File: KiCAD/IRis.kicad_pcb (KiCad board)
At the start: 2 copper layers, 31.3 x 31.3 mm, 28 parts, among them P1 Digital Out, Q1 MMBF4117, Q2 MMBF4117, Q3 MMBF4117, U1 TSV911ILT, U2 TLV3201

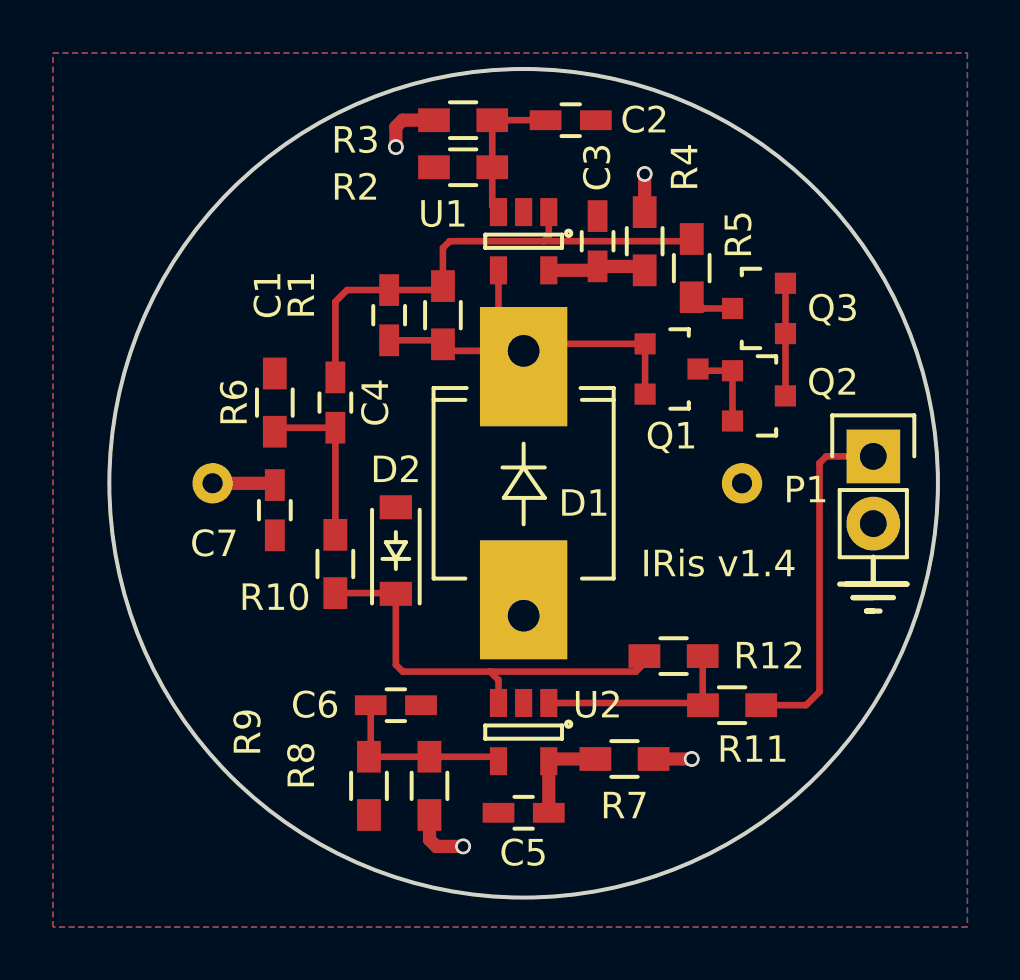
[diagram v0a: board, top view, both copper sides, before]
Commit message: Added test points TP1 and TP2 for monitoring the signal before and after DC blocking capacitor C4.
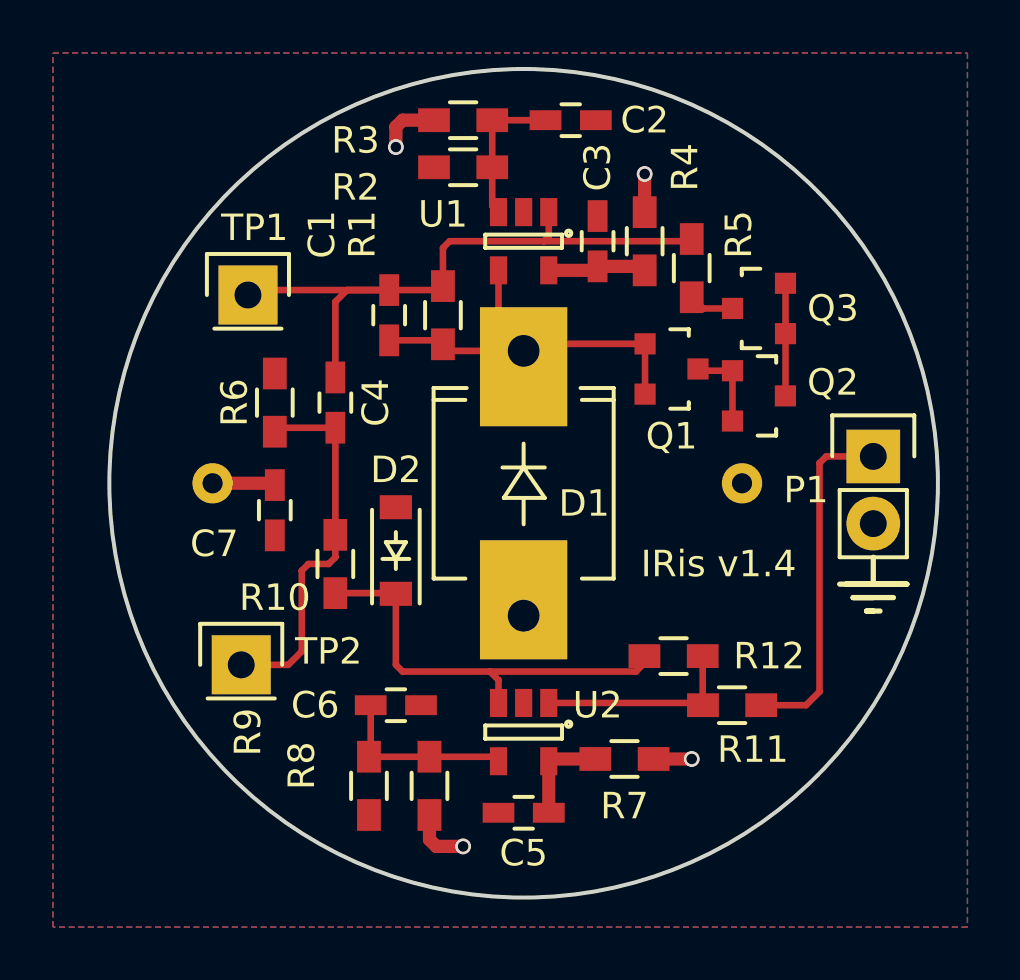
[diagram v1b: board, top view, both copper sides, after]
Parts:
- added TP1: Test Point #1, Pin_Headers:Pin_Header_Straight_1x01, F.Cu at (131.8, 92.5)
- added TP2: Test Point #2, Pin_Headers:Pin_Header_Straight_1x01, F.Cu at (131.6, 106.4)
- R5: value 100 -> 0
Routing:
- net Net-(C4-Pad1): track 6.39 -> 14.3 mm
- net Net-(C1-Pad1): track 19.6 -> 25.1 mm
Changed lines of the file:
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@@
 (kicad_pcb (version 4) (host pcbnew 4.0.2-stable)
   (general
-    (links 50)
+    (links 52)
     (no_connects 0)
     (area 124.46 82.827 159.794429 116.332001)
     (thickness 1.6)
     (drawings 15)
-    (tracks 92)
+    (tracks 101)
     (zones 0)
-    (modules 28)
+    (modules 30)
     (nets 16)
   )
@@
     (tags "capacitor 0603")
     (attr smd)
-    (fp_text reference C1 (at -0.762 4.572 270) (layer F.SilkS)
+    (fp_text reference C1 (at -3.048 2.54 270) (layer F.SilkS)
       (effects (font (size 1 1) (thickness 0.15)))
     )
@@
     (tags "resistor 0603")
     (attr smd)
-    (fp_text reference R1 (at -0.762 5.334 270) (layer F.SilkS)
+    (fp_text reference R1 (at -3.048 3.048 270) (layer F.SilkS)
       (effects (font (size 1 1) (thickness 0.15)))
     )
@@
       (effects (font (size 1 1) (thickness 0.15)))
     )
-    (fp_text value 100 (at 0 1.9 90) (layer F.Fab)
+    (fp_text value 0 (at 0 1.9 90) (layer F.Fab)
       (effects (font (size 1 1) (thickness 0.15)))
     )
@@
     )
   )
+  (module Pin_Headers:Pin_Header_Straight_1x01 (layer F.Cu)
+    (at 131.826 92.456)
+    (descr "Through hole pin header")
+    (tags "pin header")
+    (fp_text reference TP1 (at 0.254 -2.54) (layer F.SilkS)
+      (effects (font (size 1 1) (thickness 0.15)))
+    )
+    (fp_text value "Test Point #1" (at 0 -3.1) (layer F.Fab)
+      (effects (font (size 1 1) (thickness 0.15)))
+    )
+    (fp_line (start 1.55 -1.55) (end 1.55 0) (layer F.SilkS) (width 0.15))
+    (fp_line (start -1.75 -1.75) (end -1.75 1.75) (layer F.CrtYd) (width 0.05))
+    (fp_line (start 1.75 -1.75) (end 1.75 1.75) (layer F.CrtYd) (width 0.05))
+    (fp_line (start -1.75 -1.75) (end 1.75 -1.75) (layer F.CrtYd) (width 0.05))
+    (fp_line (start -1.75 1.75) (end 1.75 1.75) (layer F.CrtYd) (width 0.05))
+    (fp_line (start -1.55 0) (end -1.55 -1.55) (layer F.SilkS) (width 0.15))
+    (fp_line (start -1.55 -1.55) (end 1.55 -1.55) (layer F.SilkS) (width 0.15))
+    (fp_line (start -1.27 1.27) (end 1.27 1.27) (layer F.SilkS) (width 0.15))
+    (pad 1 thru_hole rect (at 0 0) (size 2.2352 2.2352) (drill 1.016) (layers *.Cu *.Mask F.SilkS)
+      (net 1 "Net-(C1-Pad1)"))
+    (model Pin_Headers.3dshapes/Pin_Header_Straight_1x01.wrl
+      (at (xyz 0 0 0))
+      (scale (xyz 1 1 1))
+      (rotate (xyz 0 0 90))
+    )
+  )
+  (module Pin_Headers:Pin_Header_Straight_1x01 (layer F.Cu)
+    (at 131.572 106.426)
+    (descr "Through hole pin header")
+    (tags "pin header")
+    (fp_text reference TP2 (at 3.302 -0.508) (layer F.SilkS)
+      (effects (font (size 1 1) (thickness 0.15)))
+    )
+    (fp_text value "Test Point #2" (at 0 -3.1) (layer F.Fab)
+      (effects (font (size 1 1) (thickness 0.15)))
+    )
+    (fp_line (start 1.55 -1.55) (end 1.55 0) (layer F.SilkS) (width 0.15))
+    (fp_line (start -1.75 -1.75) (end -1.75 1.75) (layer F.CrtYd) (width 0.05))
+    (fp_line (start 1.75 -1.75) (end 1.75 1.75) (layer F.CrtYd) (width 0.05))
+    (fp_line (start -1.75 -1.75) (end 1.75 -1.75) (layer F.CrtYd) (width 0.05))
+    (fp_line (start -1.75 1.75) (end 1.75 1.75) (layer F.CrtYd) (width 0.05))
+    (fp_line (start -1.55 0) (end -1.55 -1.55) (layer F.SilkS) (width 0.15))
+    (fp_line (start -1.55 -1.55) (end 1.55 -1.55) (layer F.SilkS) (width 0.15))
+    (fp_line (start -1.27 1.27) (end 1.27 1.27) (layer F.SilkS) (width 0.15))
+    (pad 1 thru_hole rect (at 0 0) (size 2.2352 2.2352) (drill 1.016) (layers *.Cu *.Mask F.SilkS)
+      (net 6 "Net-(C4-Pad1)"))
+    (model Pin_Headers.3dshapes/Pin_Header_Straight_1x01.wrl
+      (at (xyz 0 0 0))
+      (scale (xyz 1 1 1))
+      (rotate (xyz 0 0 90))
+    )
+  )
   (gr_line (start 155.194 104.394) (end 155.702 104.394) (angle 90) (layer B.SilkS) (width 0.2))
   (gr_line (start 156.21 103.886) (end 154.686 103.886) (angle 90) (layer B.SilkS) (width 0.2))
@@
   )
   (gr_circle (center 142.24 99.568) (end 154.94 108.712) (layer Edge.Cuts) (width 0.15))
+  (segment (start 137.16 92.268) (end 132.014 92.268) (width 0.25) (layer F.Cu) (net 1) (status C00000))
+  (segment (start 132.014 92.268) (end 131.826 92.456) (width 0.25) (layer F.Cu) (net 1) (status C00000))
   (segment (start 137.16 92.268) (end 135.57 92.268) (width 0.25) (layer F.Cu) (net 1))
   (segment (start 135.128 92.71) (end 135.128 95.57) (width 0.25) (layer F.Cu) (net 1))
@@
   (segment (start 144.884 91.524) (end 145.034 91.374) (width 0.5) (layer F.Cu) (net 5))
   (segment (start 143.34 91.374) (end 143.19 91.524) (width 0.25) (layer F.Cu) (net 5))
+  (segment (start 131.572 106.426) (end 133.35 106.426) (width 0.25) (layer F.Cu) (net 6) (status 400000))
+  (segment (start 135.128 102.362) (end 135.128 101.516) (width 0.25) (layer F.Cu) (net 6) (status 800000))
+  (segment (start 134.874 102.616) (end 135.128 102.362) (width 0.25) (layer F.Cu) (net 6))
+  (segment (start 134.112 102.616) (end 134.874 102.616) (width 0.25) (layer F.Cu) (net 6))
+  (segment (start 133.858 102.87) (end 134.112 102.616) (width 0.25) (layer F.Cu) (net 6))
+  (segment (start 133.858 105.918) (end 133.858 102.87) (width 0.25) (layer F.Cu) (net 6))
+  (segment (start 133.35 106.426) (end 133.858 105.918) (width 0.25) (layer F.Cu) (net 6))
   (segment (start 135.128 97.47) (end 132.992 97.47) (width 0.25) (layer F.Cu) (net 6))
   (segment (start 132.992 97.47) (end 132.842 97.62) (width 0.25) (layer F.Cu) (net 6))

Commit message: Removed all vias from volterra PCB design
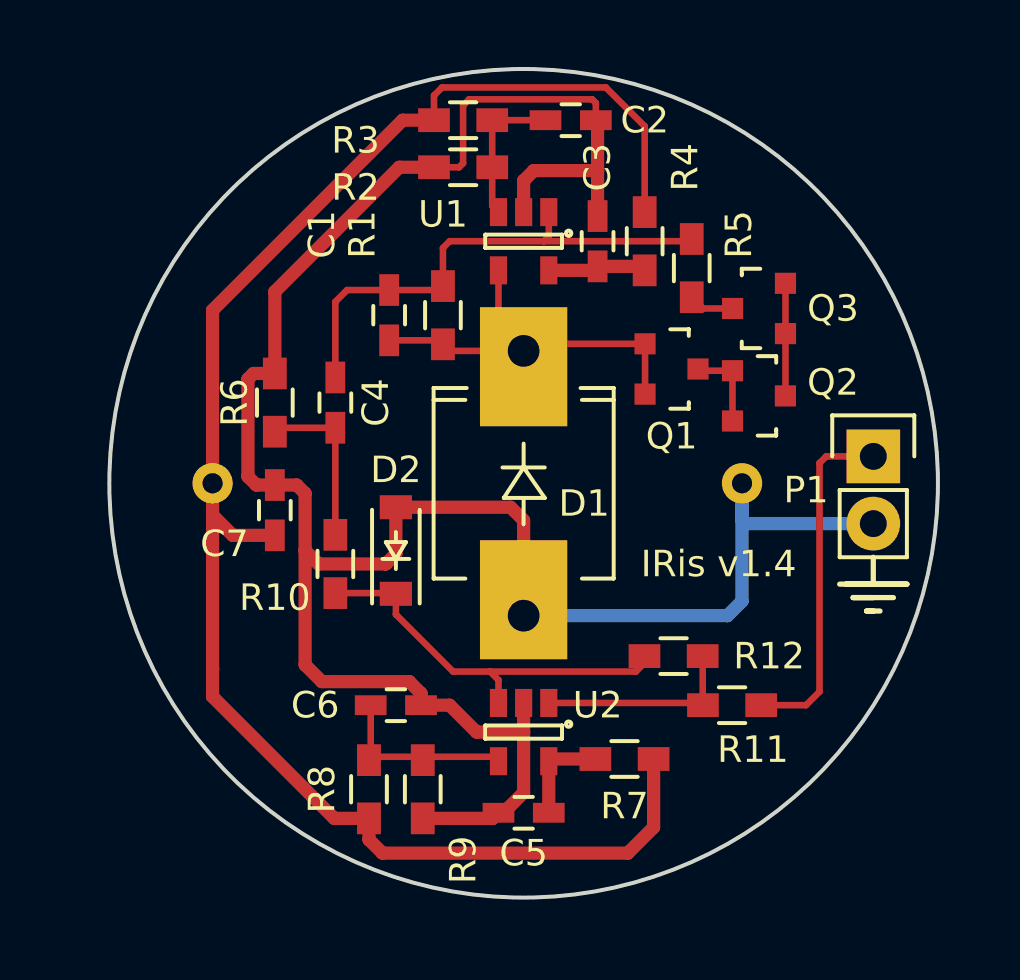
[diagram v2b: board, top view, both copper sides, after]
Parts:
- removed TP1: Test Point #1, Pin_Headers:Pin_Header_Straight_1x01
- removed TP2: Test Point #2, Pin_Headers:Pin_Header_Straight_1x01
- moved R8 2.29 mm to (136.4, 111.1)
- moved R9 2.04 mm to (138.4, 111.1)
- turned C7 to 90 degrees
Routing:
- net GND: track 0.00 -> 92.6 mm
- net +5V: track 10.1 -> 64.2 mm, vias 4 -> 0
- net Net-(C4-Pad1): track 14.3 -> 6.39 mm
- net Net-(C1-Pad1): track 25.1 -> 19.6 mm
- net Net-(D2-Pad1): track 16.7 -> 15.6 mm
- removed copper zone on B.Cu, net +5V
- removed copper zone on F.Cu, net GND
